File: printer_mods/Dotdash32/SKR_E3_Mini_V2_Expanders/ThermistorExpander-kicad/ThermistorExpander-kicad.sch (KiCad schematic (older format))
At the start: 7 parts, among them J1 Conn_02x03_Counter_Clockwise, J2 Conn_01x02, J3 Conn_01x02, J4 Conn_01x02

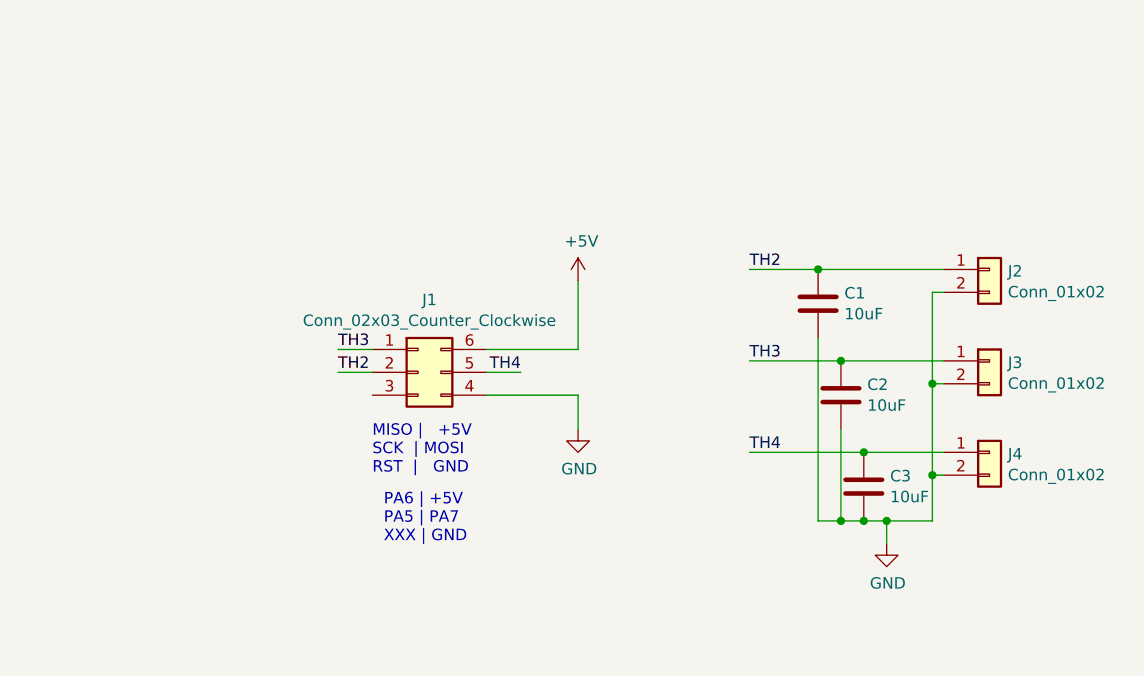
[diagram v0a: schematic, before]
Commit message: feat: PCB init layout and 3d connector models
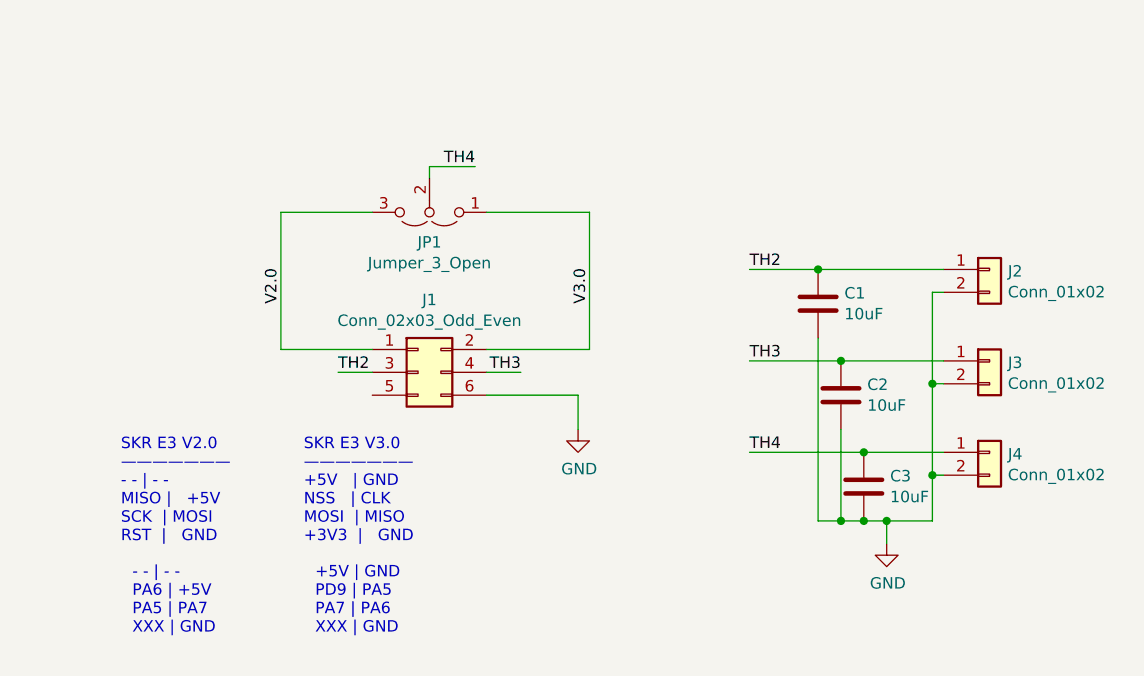
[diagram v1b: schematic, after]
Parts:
- removed C1, C2, C3: 10uF, symbol ME218_BaseLib:Cap
- removed J1: Conn_02x03_Counter_Clockwise, symbol Connector_Generic:Conn_02x03_Counter_Clockwise
- added C1, C2, C3: 10uF, Capacitors_SMD:C_0805_HandSoldering, symbol Device:C
- added J1: Conn_02x03_Odd_Even, Pin_Headers:Pin_Header_Straight_2x03_Pitch2.54mm, symbol Connector_Generic:Conn_02x03_Odd_Even
- added JP1: Jumper_3_Open, Jumper:SolderJumper-3_P1.3mm_Open_Pad1.0x1.5mm, symbol Jumper:Jumper_3_Open
- J2, J3, J4: footprint (none) -> Connectors_JST:JST_XH_S02B-XH-A_02x2.50mm_Angled
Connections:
- net GND: now also C1.2, C2.2, C3.2, J1.6 (Pin_6)
- net TH2: now also C1.1, J1.3 (Pin_3)
- net TH3: now also C2.1, J1.4 (Pin_4)
- net TH4: now also C3.1, JP1.2 (C)
- new net V2.0: J1.1 (Pin_1), JP1.3 (B)
- new net V3.0: J1.2 (Pin_2), JP1.1 (A)
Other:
- note added: "+5V | GND\nPD9 | PA5\nPA7 | PA6\nXXX | GND"
- note added: "- - | - - \nPA6 | +5V\nPA5 | PA7\nXXX | GND"
- note added: "SKR E3 V2.0\n———————\n- - | - -\nMISO | +5V\nSCK | MOSI\nRST | GND"
- note added: "SKR E3 V3.0\n———————\n+5V | GND\nNSS | CLK\nMOSI | MISO\n+3V3 | GND"
- note removed: "MISO | +5V\nSCK | MOSI\nRST | GND"
- note removed: "PA6 | +5V\nPA5 | PA7\nXXX | GND"
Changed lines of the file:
@@
 Comment4 ""
 $EndDescr
-$Comp
-L Connector_Generic:Conn_02x03_Counter_Clockwise J1
-U 1 1 61A0A579
-P 2250 2050
-F 0 "J1" H 2300 2367 50  0000 C CNN
-F 1 "Conn_02x03_Counter_Clockwise" H 2300 2276 50  0000 C CNN
-F 2 "" H 2250 2050 50  0001 C CNN
-F 3 "~" H 2250 2050 50  0001 C CNN
-	1    2250 2050
-	1    0    0    -1
-$EndComp
-Text Notes 2050 2500 0    50   ~ 0
-MISO |   +5V\nSCK  | MOSI\nRST  |   GND
-$Comp
-L power:+5V #PWR01
-U 1 1 61A0BF14
-P 2950 1650
-F 0 "#PWR01" H 2950 1500 50  0001 C CNN
-F 1 "+5V" H 2965 1823 50  0000 C CNN
-F 2 "" H 2950 1650 50  0001 C CNN
-F 3 "" H 2950 1650 50  0001 C CNN
-	1    2950 1650
-	1    0    0    -1
-$EndComp
+Text Notes 950  2800 0    50   ~ 0
+SKR E3 V2.0\n———————\n- - | - -\nMISO |   +5V\nSCK  | MOSI\nRST  |   GND
 $Comp
 L power:GND #PWR02
@@
 	2950 2150 2950 2300
 Wire Wire Line
-	2950 1650 2950 1950
-Wire Wire Line
-	2950 1950 2550 1950
-Wire Wire Line
-	2050 1950 1900 1950
-Wire Wire Line
 	2050 2050 1900 2050
 Wire Wire Line
@@
 TH2
 Text Label 2700 2050 2    50   ~ 0
-TH4
+TH3
 $Comp
 L Connector_Generic:Conn_01x02 J2
@@
 F 0 "J2" H 4830 1592 50  0000 L CNN
 F 1 "Conn_01x02" H 4830 1501 50  0000 L CNN
-F 2 "" H 4750 1600 50  0001 C CNN
+F 2 "Connectors_JST:JST_XH_S02B-XH-A_02x2.50mm_Angled" H 4750 1600 50  0001 C CNN
 F 3 "~" H 4750 1600 50  0001 C CNN
 	1    4750 1600
@@
 F 0 "J3" H 4830 1992 50  0000 L CNN
 F 1 "Conn_01x02" H 4830 1901 50  0000 L CNN
-F 2 "" H 4750 2000 50  0001 C CNN
+F 2 "Connectors_JST:JST_XH_S02B-XH-A_02x2.50mm_Angled" H 4750 2000 50  0001 C CNN
 F 3 "~" H 4750 2000 50  0001 C CNN
 	1    4750 2000
@@
 F 0 "J4" H 4830 2392 50  0000 L CNN
 F 1 "Conn_01x02" H 4830 2301 50  0000 L CNN
-F 2 "" H 4750 2400 50  0001 C CNN
+F 2 "Connectors_JST:JST_XH_S02B-XH-A_02x2.50mm_Angled" H 4750 2400 50  0001 C CNN
 F 3 "~" H 4750 2400 50  0001 C CNN
 	1    4750 2400
 	1    0    0    -1
 $EndComp
-$Comp
-L ME218_BaseLib:Cap C1
-U 1 1 61A1232B
-P 4000 1750
-F 0 "C1" H 4115 1796 50  0000 L CNN
-F 1 "10uF" H 4115 1705 50  0000 L CNN
-F 2 "" H 4038 1600 50  0001 C CNN
-F 3 "" H 4000 1750 50  0001 C CNN
-	1    4000 1750
-	1    0    0    -1
-$EndComp
-$Comp
-L ME218_BaseLib:Cap C2
-U 1 1 61A1355C
-P 4100 2150
-F 0 "C2" H 4215 2196 50  0000 L CNN
-F 1 "10uF" H 4215 2105 50  0000 L CNN
-F 2 "" H 4138 2000 50  0001 C CNN
-F 3 "" H 4100 2150 50  0001 C CNN
-	1    4100 2150
-	1    0    0    -1
-$EndComp
-$Comp
-L ME218_BaseLib:Cap C3
-U 1 1 61A14AC7
-P 4200 2550
-F 0 "C3" H 4315 2596 50  0000 L CNN
-F 1 "10uF" H 4315 2505 50  0000 L CNN
-F 2 "" H 4238 2400 50  0001 C CNN
-F 3 "" H 4200 2550 50  0001 C CNN
-	1    4200 2550
-	1    0    0    -1
-$EndComp
 Wire Wire Line
 	4000 2700 4100 2700
@@
 Connection ~ 4100 2700
 Wire Wire Line
-	4100 2700 4200 2700
-Wire Wire Line
-	4000 1600 4550 1600
-Wire Wire Line
-	4100 2000 4550 2000
-Wire Wire Line
-	4200 2400 4550 2400
-Wire Wire Line
 	4550 1700 4500 1700
 Wire Wire Line
@@
 Wire Wire Line
 	4500 2700 4300 2700
-Connection ~ 4200 2700
 Wire Wire Line
 	4550 2100 4500 2100
@@
 	4300 2800 4300 2700
 Connection ~ 4300 2700
-Wire Wire Line
-	4300 2700 4200 2700
-Wire Wire Line
-	4000 1600 3700 1600
-Connection ~ 4000 1600
-Wire Wire Line
-	4100 2000 3700 2000
-Connection ~ 4100 2000
-Wire Wire Line
-	4200 2400 3700 2400
-Connection ~ 4200 2400
 Text Label 3700 1600 0    50   ~ 0
 TH2
@@
 Text Label 3700 2400 0    50   ~ 0
 TH4
-Text Notes 2100 2800 0    50   ~ 0
-PA6 | +5V\nPA5 | PA7\nXXX | GND
-Text Label 1900 1950 0    50   ~ 0
-TH3
+Text Notes 1000 3200 0    50   ~ 0
+- - | - - \nPA6 | +5V\nPA5 | PA7\nXXX | GND
+Text Notes 1750 2800 0    50   ~ 0
+SKR E3 V3.0\n———————\n+5V   | GND\nNSS   | CLK\nMOSI  | MISO\n+3V3  |   GND
+Text Notes 1800 3200 0    50   ~ 0
++5V | GND\nPD9 | PA5\nPA7 | PA6\nXXX | GND
+$Comp
+L Jumper:Jumper_3_Open JP1
+U 1 1 61B9AB20
+P 2300 1350
+F 0 "JP1" H 2300 1481 50  0000 C CNN
+F 1 "Jumper_3_Open" H 2300 1572 50  0000 C CNN
+F 2 "Jumper:SolderJumper-3_P1.3mm_Open_Pad1.0x1.5mm" H 2300 1350 50  0001 C CNN
+F 3 "~" H 2300 1350 50  0001 C CNN
+	1    2300 1350
+	-1   0    0    1
+$EndComp
+Wire Wire Line
+	2050 1950 1650 1950
+Wire Wire Line
+	1650 1950 1650 1350
+Wire Wire Line
+	1650 1350 2050 1350
+Wire Wire Line
+	2550 1950 3000 1950
+Wire Wire Line
+	3000 1950 3000 1350
+Wire Wire Line
+	3000 1350 2550 1350
+Wire Wire Line
+	2300 1200 2300 1150
+Wire Wire Line
+	2300 1150 2500 1150
+Text Label 2500 1150 2    50   ~ 0
+TH4
+$Comp
+L Device:C C1
+U 1 1 61BA2620
+P 4000 1750
+F 0 "C1" H 4115 1796 50  0000 L CNN
+F 1 "10uF" H 4115 1705 50  0000 L CNN
+F 2 "Capacitors_SMD:C_0805_HandSoldering" H 4038 1600 50  0001 C CNN
+F 3 "~" H 4000 1750 50  0001 C CNN
+	1    4000 1750
+	1    0    0    -1
+$EndComp
+Wire Wire Line
+	3700 1600 4000 1600
+Wire Wire Line
+	3700 2000 4100 2000
+Wire Wire Line
+	3700 2400 4200 2400
+Wire Wire Line
+	4100 2700 4200 2700
+Connection ~ 4000 1600
+Wire Wire Line
+	4000 1600 4550 1600
+$Comp
+L Device:C C2
+U 1 1 61BA4139
+P 4100 2150
+F 0 "C2" H 4215 2196 50  0000 L CNN
+F 1 "10uF" H 4215 2105 50  0000 L CNN
+F 2 "Capacitors_SMD:C_0805_HandSoldering" H 4138 2000 50  0001 C CNN
+F 3 "~" H 4100 2150 50  0001 C CNN
+	1    4100 2150
+	1    0    0    -1
+$EndComp
+Connection ~ 4100 2000
+Wire Wire Line
+	4100 2000 4550 2000
+$Comp
+L Device:C C3
+U 1 1 61BA4A2F
+P 4200 2550
+F 0 "C3" H 4315 2596 50  0000 L CNN
+F 1 "10uF" H 4315 2505 50  0000 L CNN
+F 2 "Capacitors_SMD:C_0805_HandSoldering" H 4238 2400 50  0001 C CNN
+F 3 "~" H 4200 2550 50  0001 C CNN
+	1    4200 2550
+	1    0    0    -1
+$EndComp
+Connection ~ 4200 2400
+Wire Wire Line
+	4200 2400 4550 2400
+Connection ~ 4200 2700
+Wire Wire Line
+	4200 2700 4300 2700
+$Comp
+L Connector_Generic:Conn_02x03_Odd_Even J1
+U 1 1 61BB4B9B
+P 2250 2050
+F 0 "J1" H 2300 2367 50  0000 C CNN
+F 1 "Conn_02x03_Odd_Even" H 2300 2276 50  0000 C CNN
+F 2 "Pin_Headers:Pin_Header_Straight_2x03_Pitch2.54mm" H 2250 2050 50  0001 C CNN
+F 3 "~" H 2250 2050 50  0001 C CNN
+	1    2250 2050
+	1    0    0    -1
+$EndComp
+Text Label 1650 1750 1    50   ~ 0
+V2.0
+Text Label 3000 1750 1    50   ~ 0
+V3.0
 $EndSCHEMATC

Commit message: feat: use straight JSTs, clear existing SKR ports
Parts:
- C1, C2, C3: footprint Capacitors_SMD:C_0805_HandSoldering -> Capacitors_THT:C_Disc_D5.0mm_W2.5mm_P2.50mm
- J2, J3, J4: footprint Connectors_JST:JST_XH_S02B-XH-A_02x2.50mm_Angled -> Connectors_JST:JST_XH_B02B-XH-A_02x2.50mm_Straight
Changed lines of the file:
@@
 F 0 "J2" H 4830 1592 50  0000 L CNN
 F 1 "Conn_01x02" H 4830 1501 50  0000 L CNN
-F 2 "Connectors_JST:JST_XH_S02B-XH-A_02x2.50mm_Angled" H 4750 1600 50  0001 C CNN
+F 2 "Connectors_JST:JST_XH_B02B-XH-A_02x2.50mm_Straight" H 4750 1600 50  0001 C CNN
 F 3 "~" H 4750 1600 50  0001 C CNN
 	1    4750 1600
@@
 F 0 "J3" H 4830 1992 50  0000 L CNN
 F 1 "Conn_01x02" H 4830 1901 50  0000 L CNN
-F 2 "Connectors_JST:JST_XH_S02B-XH-A_02x2.50mm_Angled" H 4750 2000 50  0001 C CNN
+F 2 "Connectors_JST:JST_XH_B02B-XH-A_02x2.50mm_Straight" H 4750 2000 50  0001 C CNN
 F 3 "~" H 4750 2000 50  0001 C CNN
 	1    4750 2000
@@
 F 0 "J4" H 4830 2392 50  0000 L CNN
 F 1 "Conn_01x02" H 4830 2301 50  0000 L CNN
-F 2 "Connectors_JST:JST_XH_S02B-XH-A_02x2.50mm_Angled" H 4750 2400 50  0001 C CNN
+F 2 "Connectors_JST:JST_XH_B02B-XH-A_02x2.50mm_Straight" H 4750 2400 50  0001 C CNN
 F 3 "~" H 4750 2400 50  0001 C CNN
 	1    4750 2400
@@
 F 0 "C1" H 4115 1796 50  0000 L CNN
 F 1 "10uF" H 4115 1705 50  0000 L CNN
-F 2 "Capacitors_SMD:C_0805_HandSoldering" H 4038 1600 50  0001 C CNN
+F 2 "Capacitors_THT:C_Disc_D5.0mm_W2.5mm_P2.50mm" H 4038 1600 50  0001 C CNN
 F 3 "~" H 4000 1750 50  0001 C CNN
 	1    4000 1750
@@
 F 0 "C2" H 4215 2196 50  0000 L CNN
 F 1 "10uF" H 4215 2105 50  0000 L CNN
-F 2 "Capacitors_SMD:C_0805_HandSoldering" H 4138 2000 50  0001 C CNN
+F 2 "Capacitors_THT:C_Disc_D5.0mm_W2.5mm_P2.50mm" H 4138 2000 50  0001 C CNN
 F 3 "~" H 4100 2150 50  0001 C CNN
 	1    4100 2150
@@
 F 0 "C3" H 4315 2596 50  0000 L CNN
 F 1 "10uF" H 4315 2505 50  0000 L CNN
-F 2 "Capacitors_SMD:C_0805_HandSoldering" H 4238 2400 50  0001 C CNN
+F 2 "Capacitors_THT:C_Disc_D5.0mm_W2.5mm_P2.50mm" H 4238 2400 50  0001 C CNN
 F 3 "~" H 4200 2550 50  0001 C CNN
 	1    4200 2550

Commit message: feat|docs: 2x4 SPI header, readme updates
also re-routing some silly decisions, cleaning schematic
Also moving some readme-stuff around for
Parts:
- J1: value Conn_02x03_Odd_Even -> SPI1_breakaway; footprint Pin_Headers:Pin_Header_Straight_2x03_Pitch2.54mm -> Pin_Headers:Pin_Header_Straight_2x04_Pitch2.54mm; symbol Connector_Generic:Conn_02x03_Odd_Even -> Connector_Generic:Conn_02x04_Odd_Even
- J2, J3, J4: value Conn_01x02 -> JST-XH2
- JP1: value Jumper_3_Open -> V2-3_SEL
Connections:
- net GND: now also J1.2 (Pin_2), J1.8 (Pin_8); no longer J1.6 (Pin_6)
- net TH2: now also J1.5 (Pin_5); no longer J1.3 (Pin_3)
- net TH3: now also J1.6 (Pin_6); no longer J1.4 (Pin_4)
- net V2.0: now also J1.3 (Pin_3); no longer J1.1 (Pin_1)
- net V3.0: now also J1.4 (Pin_4); no longer J1.2 (Pin_2)
- no-connect marks 0 -> 2
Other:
- moved on the sheet: JP1
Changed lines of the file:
@@
 EELAYER 30 0
 EELAYER END
-$Descr A4 11693 8268
+$Descr A 11000 8500
 encoding utf-8
 Sheet 1 1
-Title ""
-Date ""
-Rev ""
-Comp ""
-Comment1 ""
+Title "SPI Thermistor Expander"
+Date "2022-01-08"
+Rev "1.0.1"
+Comp "Voron Design"
+Comment1 "Designed by Dotdash32 (JDeW)"
 Comment2 ""
 Comment3 ""
@@
 $EndComp
 Wire Wire Line
-	2550 2150 2950 2150
+	2550 2150 2850 2150
 Wire Wire Line
 	2950 2150 2950 2300
@@
 P 4750 1600
 F 0 "J2" H 4830 1592 50  0000 L CNN
-F 1 "Conn_01x02" H 4830 1501 50  0000 L CNN
+F 1 "JST-XH2" H 4830 1501 50  0000 L CNN
 F 2 "Connectors_JST:JST_XH_B02B-XH-A_02x2.50mm_Straight" H 4750 1600 50  0001 C CNN
 F 3 "~" H 4750 1600 50  0001 C CNN
@@
 P 4750 2000
 F 0 "J3" H 4830 1992 50  0000 L CNN
-F 1 "Conn_01x02" H 4830 1901 50  0000 L CNN
+F 1 "JST-XH2" H 4830 1901 50  0000 L CNN
 F 2 "Connectors_JST:JST_XH_B02B-XH-A_02x2.50mm_Straight" H 4750 2000 50  0001 C CNN
 F 3 "~" H 4750 2000 50  0001 C CNN
@@
 P 4750 2400
 F 0 "J4" H 4830 2392 50  0000 L CNN
-F 1 "Conn_01x02" H 4830 2301 50  0000 L CNN
+F 1 "JST-XH2" H 4830 2301 50  0000 L CNN
 F 2 "Connectors_JST:JST_XH_B02B-XH-A_02x2.50mm_Straight" H 4750 2400 50  0001 C CNN
 F 3 "~" H 4750 2400 50  0001 C CNN
@@
 L Jumper:Jumper_3_Open JP1
 U 1 1 61B9AB20
-P 2300 1350
-F 0 "JP1" H 2300 1481 50  0000 C CNN
-F 1 "Jumper_3_Open" H 2300 1572 50  0000 C CNN
-F 2 "Jumper:SolderJumper-3_P1.3mm_Open_Pad1.0x1.5mm" H 2300 1350 50  0001 C CNN
-F 3 "~" H 2300 1350 50  0001 C CNN
-	1    2300 1350
+P 2300 1250
+F 0 "JP1" H 2300 1381 50  0000 C CNN
+F 1 "V2-3_SEL" H 2300 1472 50  0000 C CNN
+F 2 "Jumper:SolderJumper-3_P1.3mm_Open_Pad1.0x1.5mm" H 2300 1250 50  0001 C CNN
+F 3 "~" H 2300 1250 50  0001 C CNN
+	1    2300 1250
 	-1   0    0    1
 $EndComp
@@
 	2050 1950 1650 1950
 Wire Wire Line
-	1650 1950 1650 1350
-Wire Wire Line
-	1650 1350 2050 1350
+	1650 1250 2050 1250
 Wire Wire Line
 	2550 1950 3000 1950
 Wire Wire Line
-	3000 1950 3000 1350
-Wire Wire Line
-	3000 1350 2550 1350
-Wire Wire Line
-	2300 1200 2300 1150
-Wire Wire Line
-	2300 1150 2500 1150
-Text Label 2500 1150 2    50   ~ 0
+	3000 1250 2550 1250
+Wire Wire Line
+	2300 1100 2300 1050
+Wire Wire Line
+	2300 1050 2500 1050
+Text Label 2500 1050 2    50   ~ 0
 TH4
 $Comp
@@
 	4200 2700 4300 2700
 $Comp
-L Connector_Generic:Conn_02x03_Odd_Even J1
+L Connector_Generic:Conn_02x04_Odd_Even J1
 U 1 1 61BB4B9B
-P 2250 2050
-F 0 "J1" H 2300 2367 50  0000 C CNN
-F 1 "Conn_02x03_Odd_Even" H 2300 2276 50  0000 C CNN
-F 2 "Pin_Headers:Pin_Header_Straight_2x03_Pitch2.54mm" H 2250 2050 50  0001 C CNN
-F 3 "~" H 2250 2050 50  0001 C CNN
-	1    2250 2050
+P 2250 1950
+F 0 "J1" H 2300 2267 50  0000 C CNN
+F 1 "SPI1_breakaway" H 2300 2176 50  0000 C CNN
+F 2 "Pin_Headers:Pin_Header_Straight_2x04_Pitch2.54mm" H 2250 1950 50  0001 C CNN
+F 3 "~" H 2250 1950 50  0001 C CNN
+	1    2250 1950
 	1    0    0    -1
 $EndComp
@@
 Text Label 3000 1750 1    50   ~ 0
 V3.0
+Wire Wire Line
+	1650 1250 1650 1950
+Wire Wire Line
+	3000 1250 3000 1950
+Wire Wire Line
+	2550 1850 2850 1850
+Wire Wire Line
+	2850 1850 2850 2150
+Connection ~ 2850 2150
+Wire Wire Line
+	2850 2150 2950 2150
+NoConn ~ 2050 2150
+NoConn ~ 2050 1850
 $EndSCHEMATC

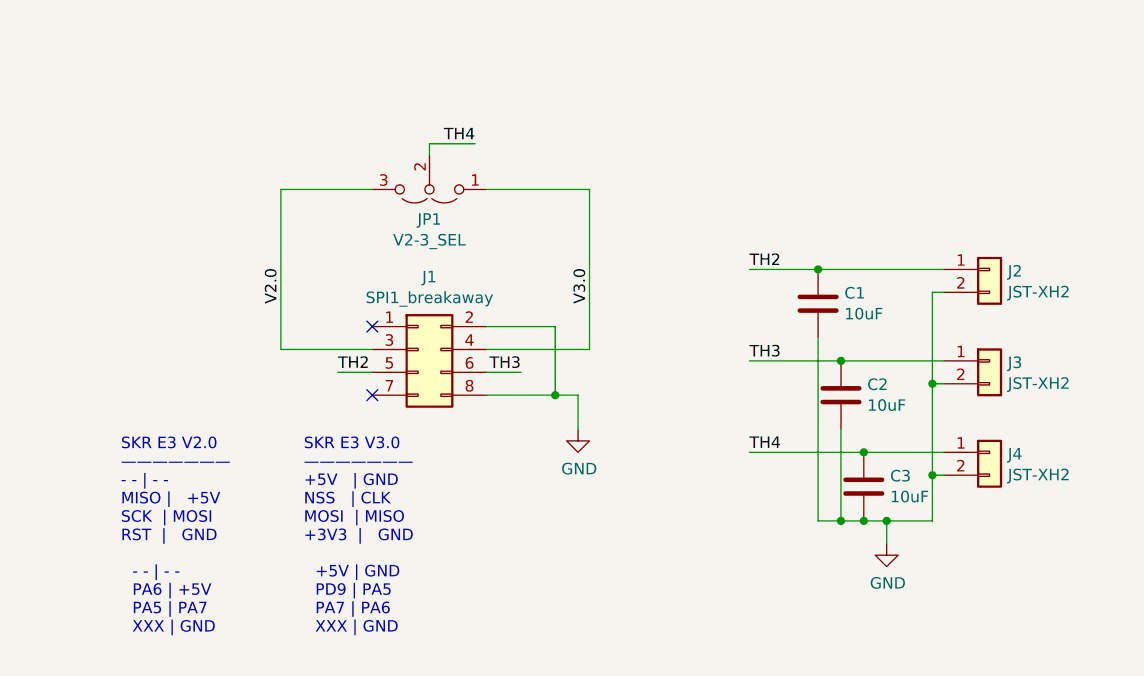
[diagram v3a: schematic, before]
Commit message: test: LCSC larger THT capacitor
it's sooo bigg though...
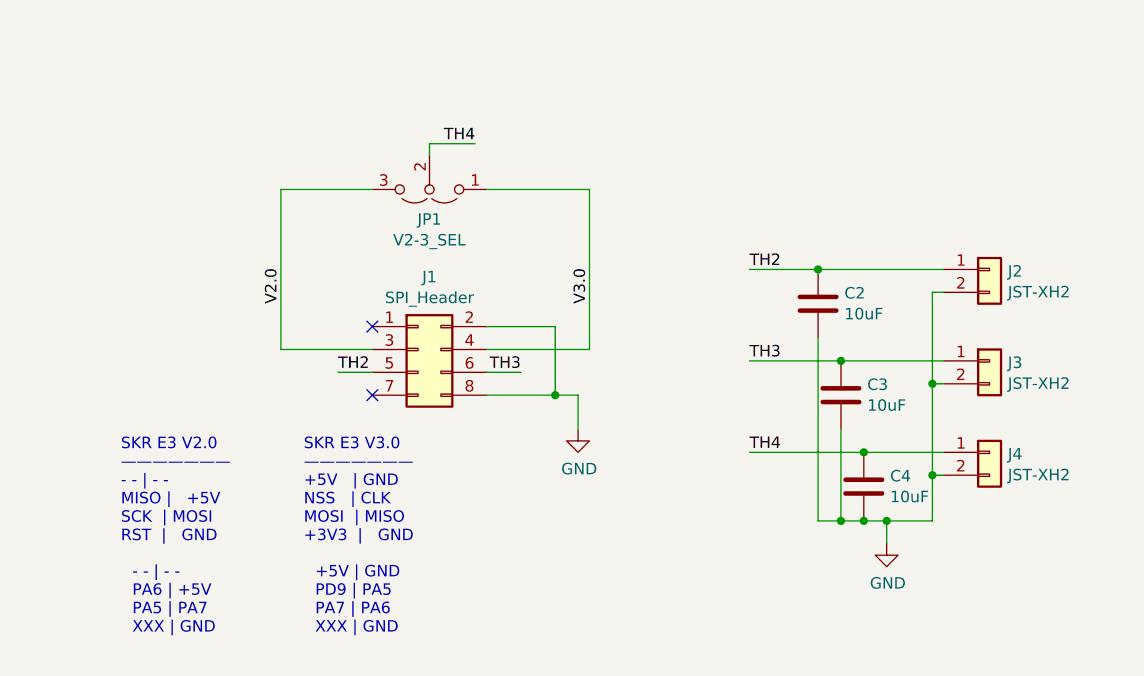
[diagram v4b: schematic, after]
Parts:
- J1: value SPI1_breakaway -> SPI_Header
- renumbered C1 to C2, C2 to C3, C3 to C4
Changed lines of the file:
@@
 TH4
 $Comp
-L Device:C C1
+L Device:C C2
 U 1 1 61BA2620
 P 4000 1750
-F 0 "C1" H 4115 1796 50  0000 L CNN
+F 0 "C2" H 4115 1796 50  0000 L CNN
 F 1 "10uF" H 4115 1705 50  0000 L CNN
 F 2 "Capacitors_THT:C_Disc_D5.0mm_W2.5mm_P2.50mm" H 4038 1600 50  0001 C CNN
@@
 	4000 1600 4550 1600
 $Comp
-L Device:C C2
+L Device:C C3
 U 1 1 61BA4139
 P 4100 2150
-F 0 "C2" H 4215 2196 50  0000 L CNN
+F 0 "C3" H 4215 2196 50  0000 L CNN
 F 1 "10uF" H 4215 2105 50  0000 L CNN
 F 2 "Capacitors_THT:C_Disc_D5.0mm_W2.5mm_P2.50mm" H 4138 2000 50  0001 C CNN
@@
 	4100 2000 4550 2000
 $Comp
-L Device:C C3
+L Device:C C4
 U 1 1 61BA4A2F
 P 4200 2550
-F 0 "C3" H 4315 2596 50  0000 L CNN
+F 0 "C4" H 4315 2596 50  0000 L CNN
 F 1 "10uF" H 4315 2505 50  0000 L CNN
 F 2 "Capacitors_THT:C_Disc_D5.0mm_W2.5mm_P2.50mm" H 4238 2400 50  0001 C CNN
@@
 P 2250 1950
 F 0 "J1" H 2300 2267 50  0000 C CNN
-F 1 "SPI1_breakaway" H 2300 2176 50  0000 C CNN
+F 1 "SPI_Header" H 2300 2176 50  0000 C CNN
 F 2 "Pin_Headers:Pin_Header_Straight_2x04_Pitch2.54mm" H 2250 1950 50  0001 C CNN
 F 3 "~" H 2250 1950 50  0001 C CNN

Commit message: feat: move to SMD capacitors for sourcing
upsetti spaghetti, THT capacitors are hard to find, so we'll just
use SMD (1206) capacitors
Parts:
- C2, C3, C4: footprint Capacitors_THT:C_Disc_D5.0mm_W2.5mm_P2.50mm -> Capacitors_SMD:C_1206_HandSoldering
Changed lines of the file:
@@
 F 0 "C2" H 4115 1796 50  0000 L CNN
 F 1 "10uF" H 4115 1705 50  0000 L CNN
-F 2 "Capacitors_THT:C_Disc_D5.0mm_W2.5mm_P2.50mm" H 4038 1600 50  0001 C CNN
+F 2 "Capacitors_SMD:C_1206_HandSoldering" H 4038 1600 50  0001 C CNN
 F 3 "~" H 4000 1750 50  0001 C CNN
 	1    4000 1750
@@
 F 0 "C3" H 4215 2196 50  0000 L CNN
 F 1 "10uF" H 4215 2105 50  0000 L CNN
-F 2 "Capacitors_THT:C_Disc_D5.0mm_W2.5mm_P2.50mm" H 4138 2000 50  0001 C CNN
+F 2 "Capacitors_SMD:C_1206_HandSoldering" H 4138 2000 50  0001 C CNN
 F 3 "~" H 4100 2150 50  0001 C CNN
 	1    4100 2150
@@
 F 0 "C4" H 4315 2596 50  0000 L CNN
 F 1 "10uF" H 4315 2505 50  0000 L CNN
-F 2 "Capacitors_THT:C_Disc_D5.0mm_W2.5mm_P2.50mm" H 4238 2400 50  0001 C CNN
+F 2 "Capacitors_SMD:C_1206_HandSoldering" H 4238 2400 50  0001 C CNN
 F 3 "~" H 4200 2550 50  0001 C CNN
 	1    4200 2550
